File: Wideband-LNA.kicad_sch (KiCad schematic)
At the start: 27 parts, among them J1 RF-IN, J2 RF-OUT, J3 USB_C_Receptacle_USB2.0_16P, U1 TQP3M9036, U2 AP2127K-ADJ

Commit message: Updated jlcpcb components
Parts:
- C1, C2, C3: value 1nF -> 330p
- L2, L5: value 680n -> 470n
- R2, R7: value 10 -> 105
- R8: value 10 -> 61.9
- U1: value TQP3M9036 -> TQP3M9037
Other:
- note added: "December 2025"
- note added: "Gain flattening Atten 9 dB at 144 MHz and below 3.8 dB at 1296 and above"
- note added: "Git Branch TQP3M9037_19x19_V3.4"
- note added: "Qorvo TQP3M9037 LNA 50 to 3000 MHz"
- note added: "uSimmics v5.8 Simulation"
- note removed: "Git Branch TQP3M9036_19x19_V3.4"
- note removed: "November, 2025"
- note removed: "Qorvo TQP3M9036 LNA 50 to 1500 MHz"
- moved on the sheet: C1, C2, C3, C4, C5, C6, C7, C8, FB1, H1, H2, H3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

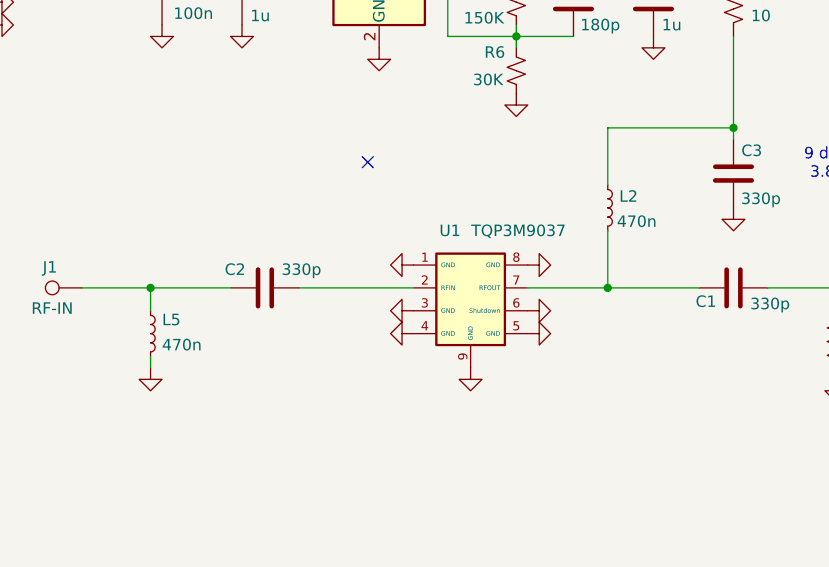
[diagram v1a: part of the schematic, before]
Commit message: Changed inductors for input antistatic and DC choke
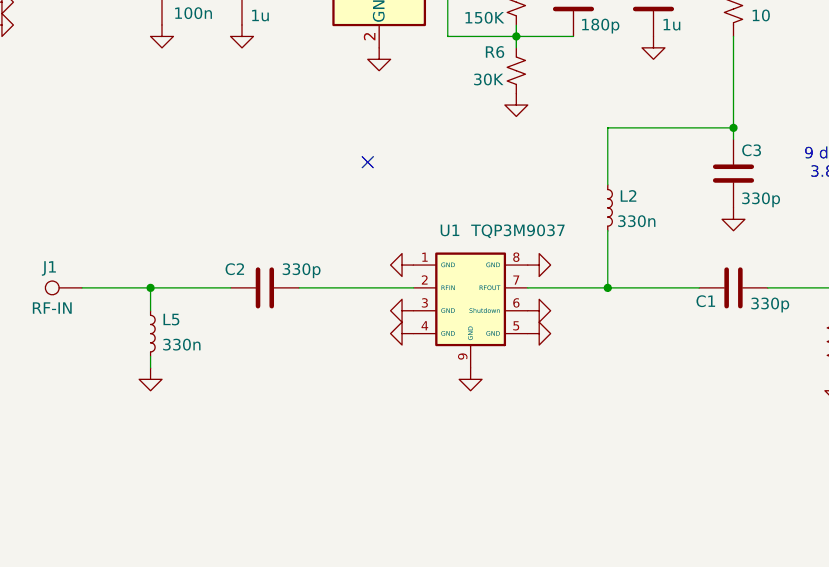
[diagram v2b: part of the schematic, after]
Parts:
- L2, L5: value 470n -> 330n

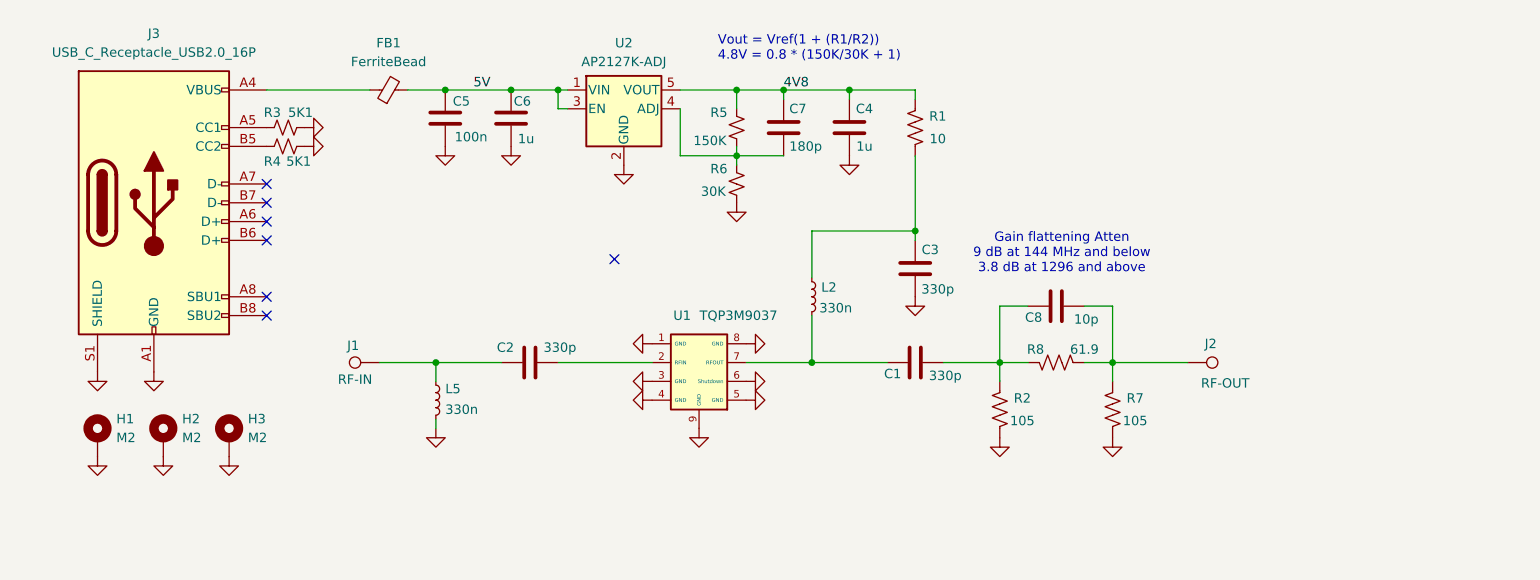
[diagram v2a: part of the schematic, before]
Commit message: added bias T changed from USB-C to feed through
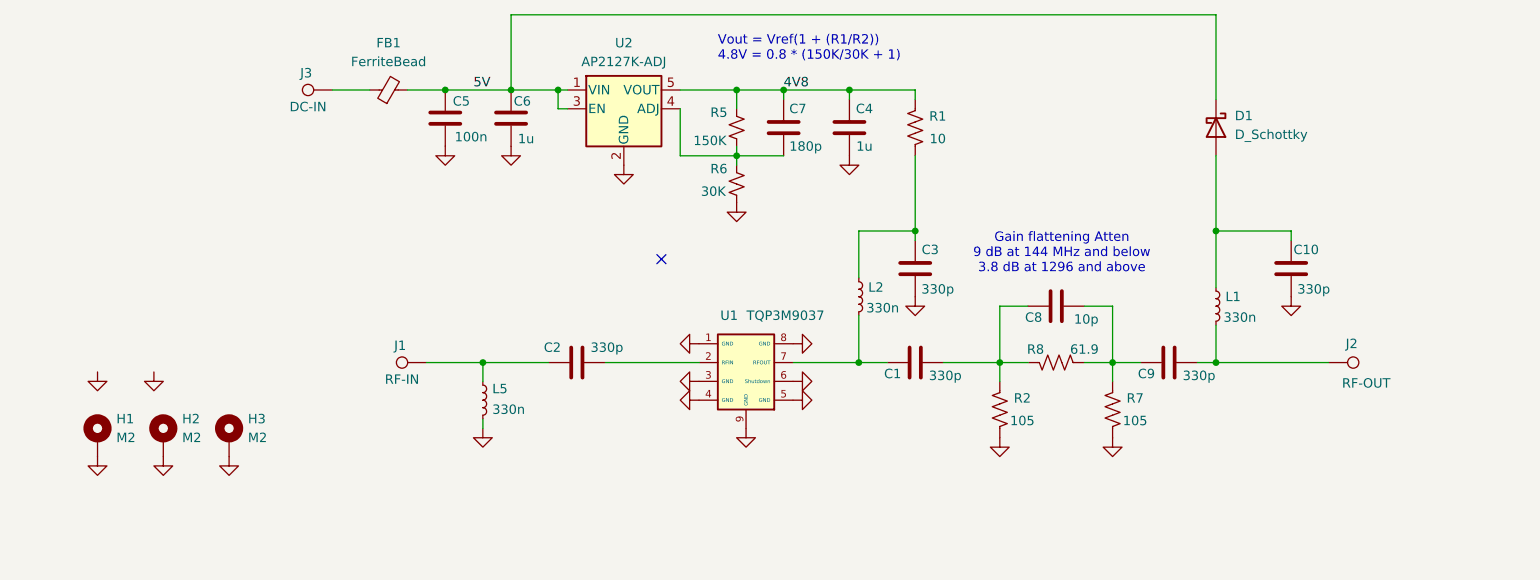
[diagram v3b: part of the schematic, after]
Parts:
- removed J3: USB_C_Receptacle_USB2.0_16P, wa1hco:USB_C_Receptacle_G-Switch_GT-USB-7010ASV, symbol Connector:USB_C_Receptacle_USB2.0_16P
- removed R3, R4: 5K1, Resistor_SMD:R_0402_1005Metric, symbol Device:R_Small_US
- added C10, C9: 330p, Capacitor_SMD:C_0402_1005Metric, symbol Device:C
- added D1: D_Schottky, Diode_SMD:D_SOD-523, symbol Device:D_Schottky
- added J3: DC-IN, TestPoint:TestPoint_Pad_1.0x1.0mm, symbol Connector:TestPoint
- added L1: 330n, Inductor_SMD:L_0603_1608Metric, symbol Device:L_Small
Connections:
- net 5V: now also D1.1 (K)
- net GND: now also C10.2
- net at C8.2, R7.1, R8.2: now also C9.1; no longer J2.1
- net at FB1.1: now also J3.1
- new net: C10.1, D1.2 (A), L1.1
- new net: C9.2, J2.1, L1.2
- no-connect marks 7 -> 1
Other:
- moved on the sheet: C2, J1, J2, L2, L5, U1

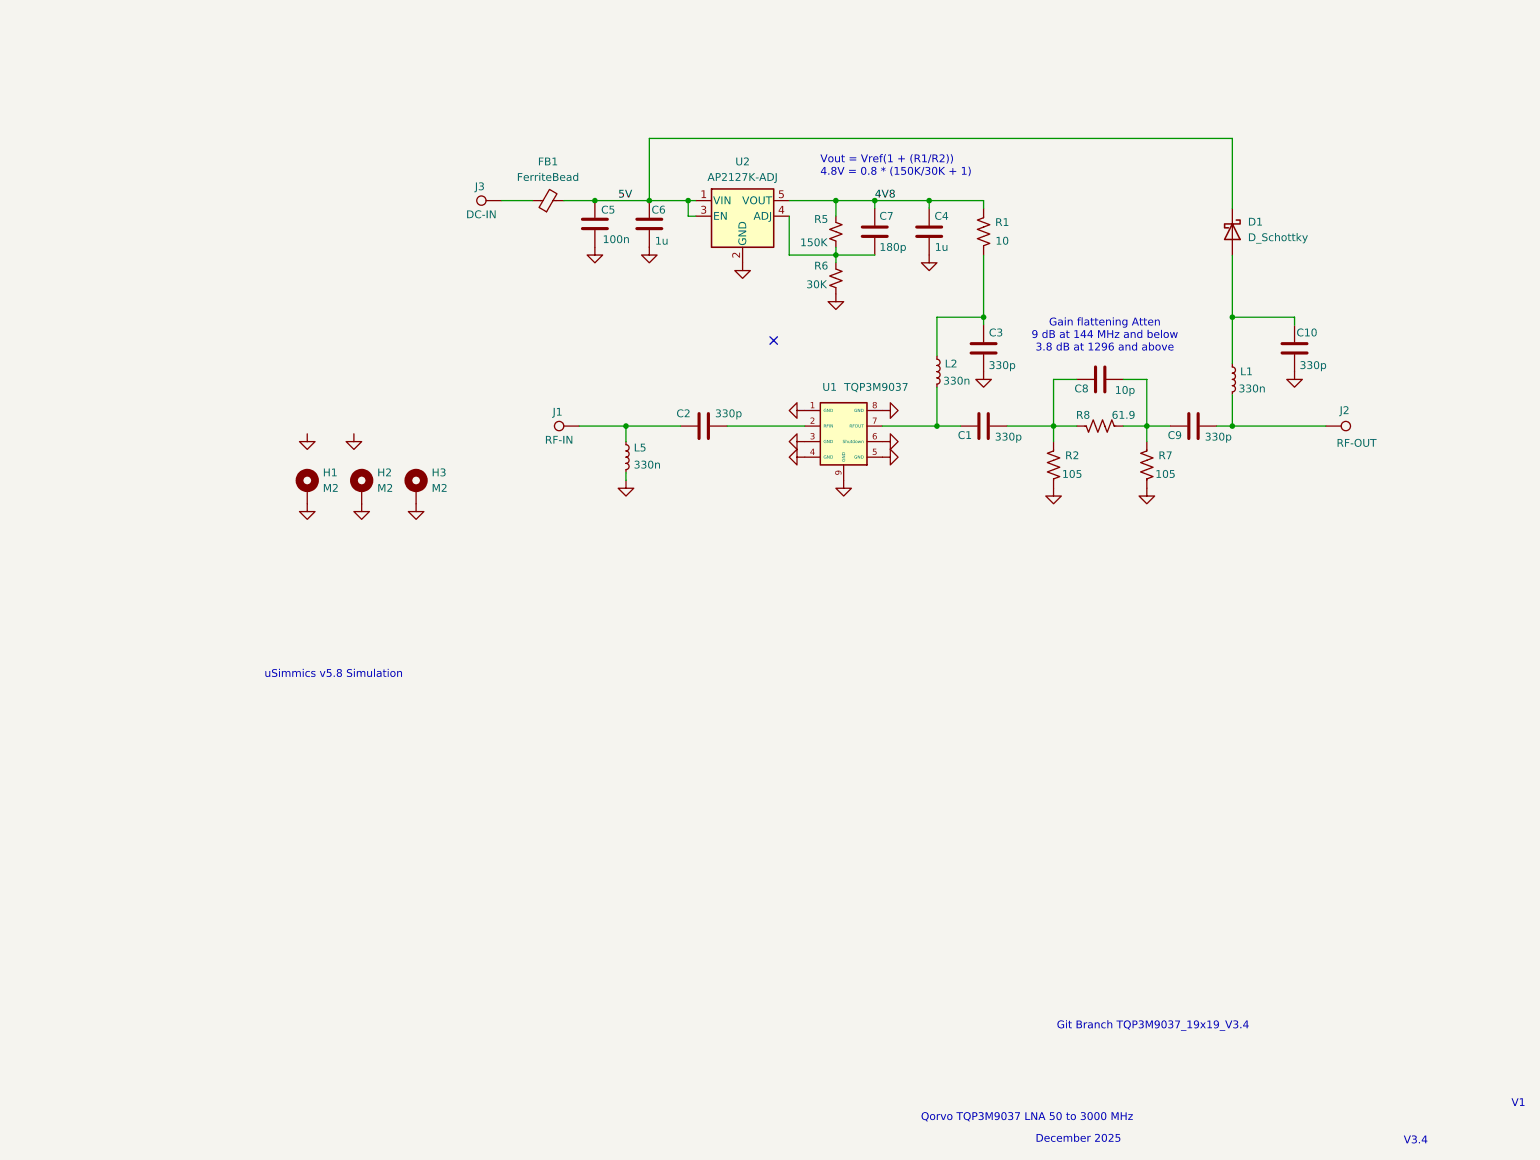
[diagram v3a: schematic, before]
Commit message: Optimize layout for 0603 components Change from USB-C to pad for feedthrough capacitor Change regulator to 78L05
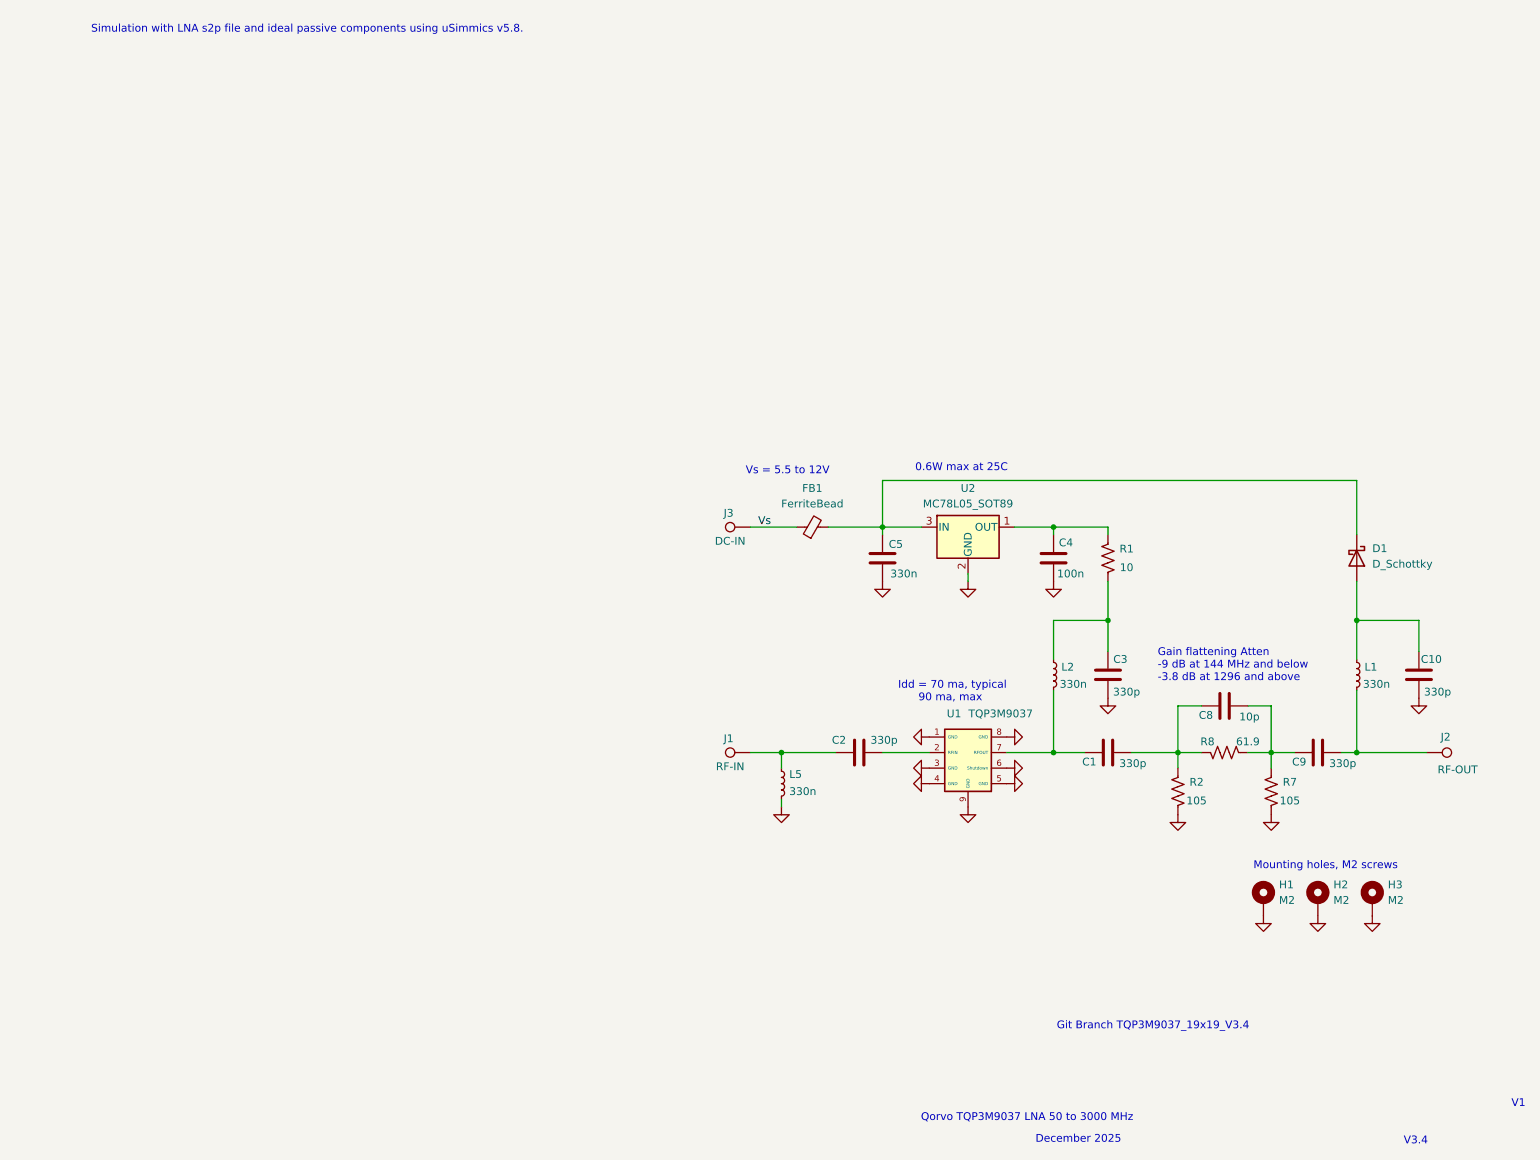
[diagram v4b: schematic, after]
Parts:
- removed C6: 1u, Capacitor_SMD:C_0402_1005Metric, symbol Device:C
- removed C7: 180p, Capacitor_SMD:C_0402_1005Metric, symbol Device:C
- removed R5: 150K, Resistor_SMD:R_0402_1005Metric, symbol Device:R_Small_US
- removed R6: 30K, Resistor_SMD:R_0402_1005Metric, symbol Device:R_Small_US
- removed U2: AP2127K-ADJ, Package_TO_SOT_SMD:SOT-23-5, symbol Regulator_Linear:AP2127K-ADJ
- added U2: MC78L05_SOT89, Package_TO_SOT_SMD:SOT-89-3, symbol Regulator_Linear:MC78L05_SOT89
- C1, C10, C2, C3, C8, C9: footprint Capacitor_SMD:C_0402_1005Metric -> Capacitor_SMD:C_0603_1608Metric
- C4: value 1u -> 100n; footprint Capacitor_SMD:C_0402_1005Metric -> Capacitor_SMD:C_0603_1608Metric
- C5: value 100n -> 330n; footprint Capacitor_SMD:C_0402_1005Metric -> Capacitor_SMD:C_0603_1608Metric
- R1, R2, R7, R8: footprint Resistor_SMD:R_0402_1005Metric -> Resistor_SMD:R_0603_1608Metric
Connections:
- net GND: now also U2.2 (GND)
- net Vs: now reaches FB1.1, J3.1
- net 4V8: no longer names the net of C4.1, R1.1
- net 4V8: now also U2.1 (OUT)
- net 5V: no longer names the net of C5.1, D1.1 (K), FB1.2
- net 5V: now also U2.3 (IN)
- no-connect marks 1 -> 0
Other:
- note added: "0.6W max at 25C"
- note added: "Gain flattening Atten -9 dB at 144 MHz and below -3.8 dB at 1296 and above"
- note added: "Idd = 70 ma, typical 90 ma, max"
- note added: "Mounting holes, M2 screws"
- note added: "Simulation with LNA s2p file and ideal passive components using uSimmics v5.8."
- note added: "Vs = 5.5 to 12V"
- note removed: "Gain flattening Atten 9 dB at 144 MHz and below 3.8 dB at 1296 and above"
- note removed: "Vout = Vref(1 + (R1/R2)) 4.8V = 0.8 * (150K/30K + 1)"
- note removed: "uSimmics v5.8 Simulation"
- moved on the sheet: C1, C10, C2, C3, C4, C5, C8, C9, D1, FB1, H1, H2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

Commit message: Relayout for 8-32 feedthrough capacitor Relayout for larger DPAK voltage regulator, allows high input voltage Had to remove 10 Ohm series resistor in LNA supply lead Reduced size of ferrite bead to 0603 Moved
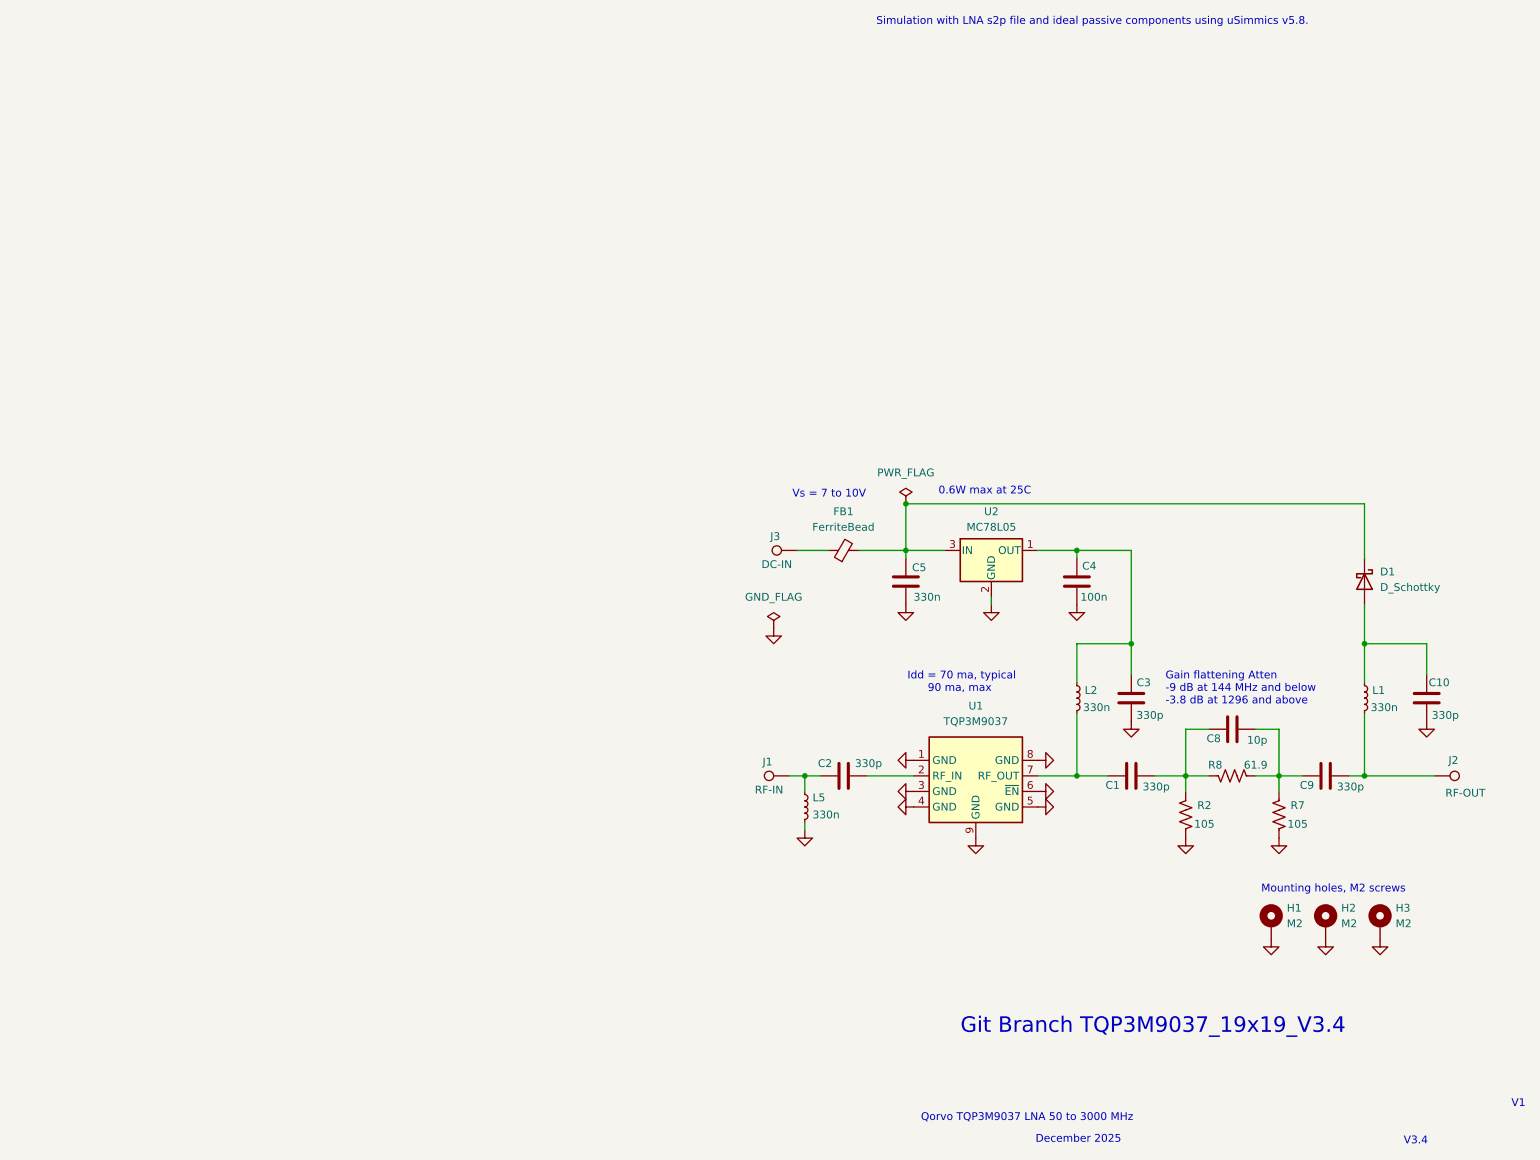
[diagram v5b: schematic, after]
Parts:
- removed R1: 10, Resistor_SMD:R_0603_1608Metric, symbol Device:R_US
- removed U1: TQP3M9037, wa1hco:DFN-8-1EP_2x2mm_P0.5mm_EP0.8x1.6mm_via, symbol wa1hco:TQP3M9036
- added U1: TQP3M9037, Package_DFN_QFN:DFN-8-1EP_2x2mm_P0.5mm_EP0.8x1.6mm, symbol wa1hco:TQP3M9037
- FB1: footprint Inductor_SMD:L_0805_2012Metric -> Inductor_SMD:L_0603_1608Metric
- U2: value MC78L05_SOT89 -> MC78L05; footprint Package_TO_SOT_SMD:SOT-89-3 -> Package_TO_SOT_SMD:TO-252-2
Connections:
- net GND: now also U1.1 (GND), U1.3 (GND), U1.4 (GND), U1.5 (GND), U1.6 (~{EN}), U1.8 (GND), U1.9 (GND)
- net at C3.1, L2.1: now also C4.1, U2.1 (OUT)
- net at C1.1, L2.2: now also U1.7 (RF_OUT)
- net at C2.2: now also U1.2 (RF_IN)
- net Vs: no longer names the net of FB1.1, J3.1
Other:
- note added: "Vs = 7 to 10V"
- note removed: "Vs = 5.5 to 12V"
- moved on the sheet: C1, C10, C2, C3, C4, C5, C8, C9, D1, FB1, H1, H2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

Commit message: Selected components for manufacturing, generated JLCPCB files
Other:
- note added: "0.9W max at 25C"
- note added: "Vs = 8 to 15V"
- note removed: "0.6W max at 25C"
- note removed: "Vs = 7 to 10V"
